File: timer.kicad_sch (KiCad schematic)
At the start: 9 parts, among them Q1 PN2222A, U33 8254, U4 74LS00, U41 74LS175

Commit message: fixed things
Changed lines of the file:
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@@
 	)
 	(hierarchical_label "PIT IRQ"
-		(shape input)
+		(shape output)
 		(at 208.28 106.68 0)
 		(effects
@@
 	)
 	(hierarchical_label "SPKR OUT"
-		(shape input)
+		(shape output)
 		(at 208.28 140.97 0)
 		(effects

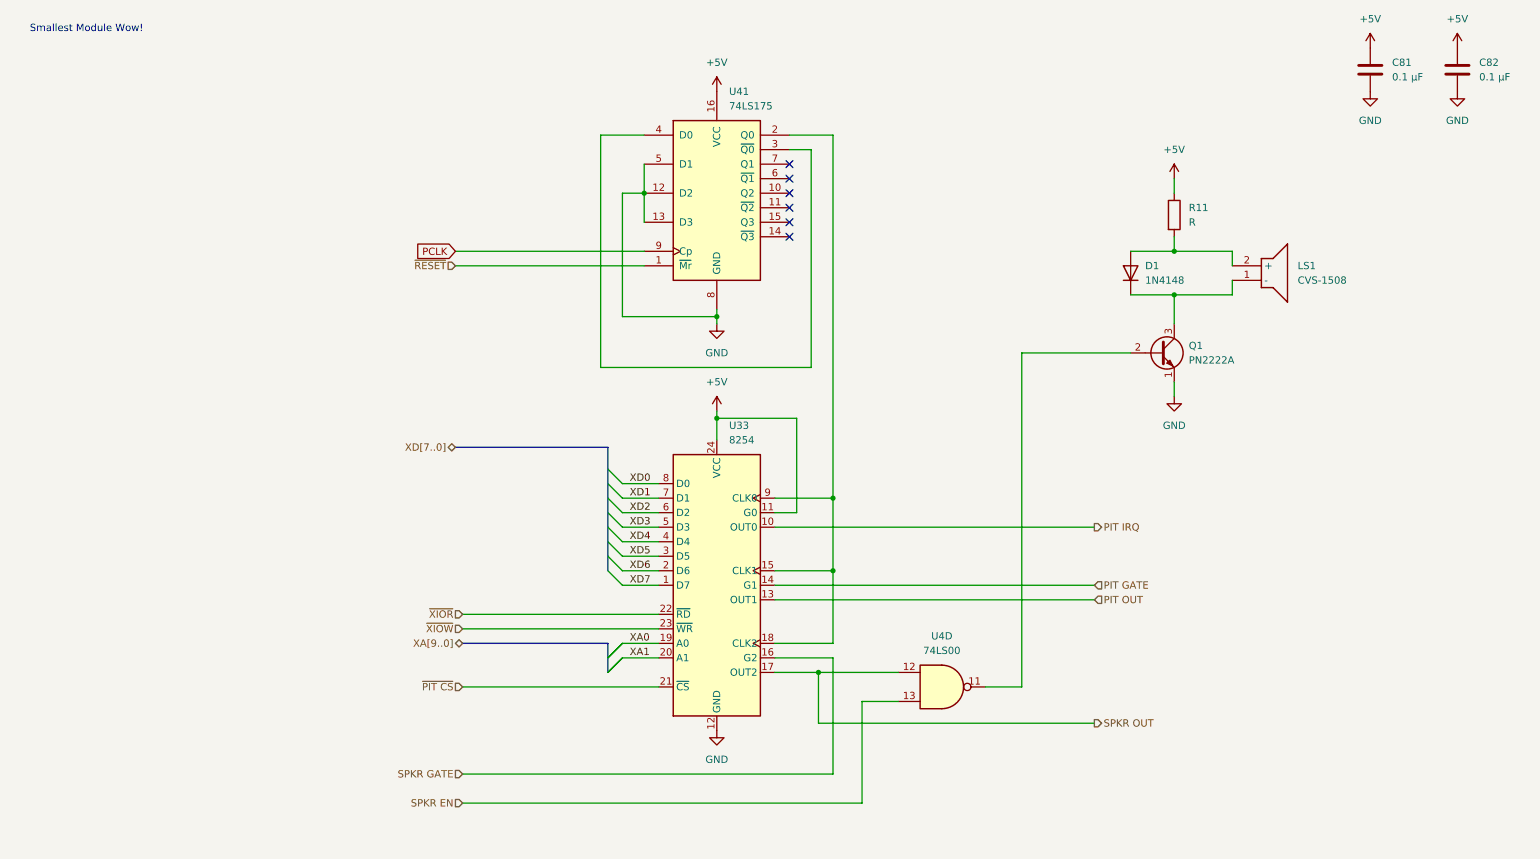
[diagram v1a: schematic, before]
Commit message: Upgraded speaker, esd protection, added dip sockets, adjusted routing
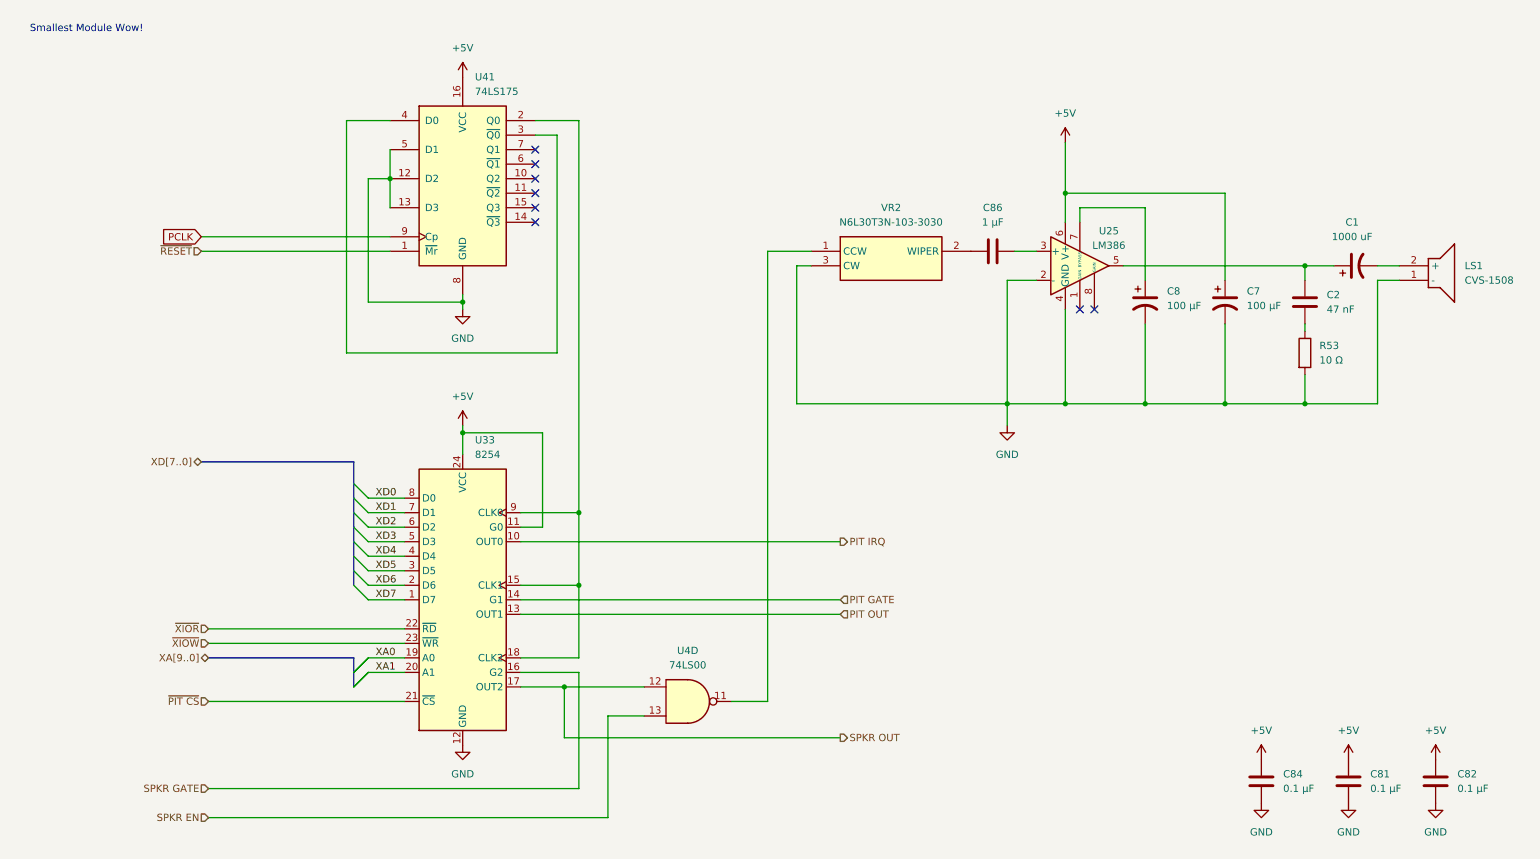
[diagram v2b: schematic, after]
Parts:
- removed D1: 1N4148, Diode_THT:D_DO-35_SOD27_P7.62mm_Horizontal, symbol Diode:1N4148
- removed Q1: PN2222A, Package_TO_SOT_THT:TO-92_Inline, symbol Transistor_BJT:PN2222A
- removed R11: R, Resistor_SMD:R_1206_3216Metric_Pad1.30x1.75mm_HandSolder, symbol Device:R
- added C1: 1000 uF, Capacitor_THT:CP_Radial_D8.0mm_P3.50mm, symbol Device:C_Polarized_US
- added C2: 47 nF, Capacitor_SMD:C_1210_3225Metric_Pad1.33x2.70mm_HandSolder, symbol Device:C
- added C7, C8: 100 μF, Capacitor_THT:CP_Radial_D6.3mm_P2.50mm, symbol Device:C_Polarized_US
- added C84: 0.1 μF, Capacitor_SMD:C_1210_3225Metric_Pad1.33x2.70mm_HandSolder, symbol Device:C
- added C86: 1 μF, Capacitor_SMD:C_1210_3225Metric_Pad1.33x2.70mm_HandSolder, symbol Device:C
- added R53: 10 Ω, Resistor_SMD:R_1206_3216Metric_Pad1.30x1.75mm_HandSolder, symbol Device:R
- added U25: LM386, Package_DIP:DIP-8_W7.62mm_Socket, symbol Amplifier_Audio:LM386
- added VR2: N6L30T3N-103-3030, Library:N6L30T3N1033030, symbol N6L30T3N-103-3030:N6L30T3N-103-3030
- U33: footprint Package_DIP:DIP-24_W15.24mm -> Package_DIP:DIP-24_W15.24mm_Socket
- U4: footprint Package_DIP:DIP-14_W7.62mm -> Package_DIP:DIP-14_W7.62mm_Socket
- U41: footprint Package_DIP:DIP-16_W7.62mm -> Package_DIP:DIP-16_W7.62mm_Socket
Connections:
- net +5V: now also C7.1, C84.1, U25.6 (V+)
- net GND: now also LS1.1 (-), C7.2, C8.2, C84.2, R53.2, U25.2 (-), U25.4 (GND), VR2.3 (CW)
- net at LS1.2 (+): now also C1.2
- net at U4.11: now also VR2.1 (CCW)
- new net: C86.1, VR2.2 (WIPER)
- new net: C86.2, U25.3 (+)
- new net: C1.1, C2.1, U25.5
- new net: C8.1, U25.7 (BYPASS)
- new net: C2.2, R53.1
- no-connect marks 6 -> 8
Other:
- moved on the sheet: C81, C82, LS1, U33, U41, U4D

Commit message: final commit before spinning
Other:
- moved on the sheet: C81, C82, C84
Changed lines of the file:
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@@
 	)
 	(junction
-		(at 85.09 45.72)
+		(at 97.79 67.31)
 		(diameter 0)
 		(color 0 0 0 0)
@@
 	)
 	(junction
-		(at 115.57 134.62)
+		(at 85.09 45.72)
 		(diameter 0)
 		(color 0 0 0 0)
 	)
 	(junction
-		(at 217.17 85.09)
+		(at 115.57 134.62)
 		(diameter 0)
 		(color 0 0 0 0)
 	)
 	(junction
-		(at 97.79 67.31)
+		(at 217.17 85.09)
 		(diameter 0)
 		(color 0 0 0 0)
@@
 	)
 	(hierarchical_label "PIT OUT"
-		(shape input)
+		(shape output)
 		(at 163.83 121.92 0)
 		(effects
@@
 	(symbol
 		(lib_id "power:GND")
-		(at 267.97 154.94 0)
+		(at 269.24 156.21 0)
 		(unit 1)
 		(body_style 1)
@@
 		(fields_autoplaced yes)
 		(property "Reference" "#PWR0272"
-			(at 267.97 161.29 0)
+			(at 269.24 162.56 0)
 			(hide yes)
 			(show_name no)
@@
 		)
 		(property "Value" "GND"
-			(at 267.97 160.02 0)
+			(at 269.24 161.29 0)
 			(show_name no)
 			(do_not_autoplace no)
@@
 		)
 		(property "Footprint" ""
-			(at 267.97 154.94 0)
+			(at 269.24 156.21 0)
 			(hide yes)
 			(show_name no)
@@
 		)
 		(property "Datasheet" ""
-			(at 267.97 154.94 0)
+			(at 269.24 156.21 0)
 			(hide yes)
 			(show_name no)
@@
 		)
 		(property "Description" "Power symbol creates a global label with name \"GND\" , ground"
-			(at 267.97 154.94 0)
+			(at 269.24 156.21 0)
 			(hide yes)
 			(show_name no)
@@
 	(symbol
 		(lib_id "power:GND")
-		(at 252.73 154.94 0)
+		(at 254 156.21 0)
 		(unit 1)
 		(body_style 1)
@@
 		(fields_autoplaced yes)
 		(property "Reference" "#PWR0270"
-			(at 252.73 161.29 0)
+			(at 254 162.56 0)
 			(hide yes)
 			(show_name no)
@@
 		)
 		(property "Value" "GND"
-			(at 252.73 160.02 0)
+			(at 254 161.29 0)
 			(show_name no)
 			(do_not_autoplace no)
@@
 		)
 		(property "Footprint" ""
-			(at 252.73 154.94 0)
+			(at 254 156.21 0)
 			(hide yes)
 			(show_name no)
@@
 		)
 		(property "Datasheet" ""
-			(at 252.73 154.94 0)
+			(at 254 156.21 0)
 			(hide yes)
 			(show_name no)
@@
 		)
 		(property "Description" "Power symbol creates a global label with name \"GND\" , ground"
-			(at 252.73 154.94 0)
+			(at 254 156.21 0)
 			(hide yes)
 			(show_name no)
@@
 	(symbol
 		(lib_id "Device:C")
-		(at 267.97 151.13 0)
+		(at 269.24 152.4 0)
 		(unit 1)
 		(body_style 1)
@@
 		(fields_autoplaced yes)
 		(property "Reference" "C82"
-			(at 271.78 149.8599 0)
+			(at 273.05 151.1299 0)
 			(show_name no)
 			(do_not_autoplace no)
@@
 		)
 		(property "Value" "0.1 μF"
-			(at 271.78 152.3999 0)
+			(at 273.05 153.6699 0)
 			(show_name no)
 			(do_not_autoplace no)
@@
 		)
 		(property "Footprint" "Capacitor_SMD:C_1210_3225Metric_Pad1.33x2.70mm_HandSolder"
-			(at 268.9352 154.94 0)
+			(at 270.2052 156.21 0)
 			(hide yes)
 			(show_name no)
@@
 		)
 		(property "Datasheet" ""
-			(at 267.97 151.13 0)
+			(at 269.24 152.4 0)
 			(hide yes)
 			(show_name no)
@@
 		)
 		(property "Description" "Unpolarized capacitor"
-			(at 267.97 151.13 0)
+			(at 269.24 152.4 0)
 			(hide yes)
 			(show_name no)
@@
 		)
 		(property "Sim.Type" ""
-			(at 267.97 151.13 0)
+			(at 269.24 152.4 0)
 			(hide yes)
 			(show_name no)
@@
 		)
 		(property "Sim.Device" ""
-			(at 267.97 151.13 0)
+			(at 269.24 152.4 0)
 			(hide yes)
 			(show_name no)
@@
 	(symbol
 		(lib_id "power:GND")
-		(at 237.49 154.94 0)
+		(at 238.76 156.21 0)
 		(unit 1)
 		(body_style 1)
@@
 		(fields_autoplaced yes)
 		(property "Reference" "#PWR0279"
-			(at 237.49 161.29 0)
+			(at 238.76 162.56 0)
 			(hide yes)
 			(show_name no)
@@
 		)
 		(property "Value" "GND"
-			(at 237.49 160.02 0)
+			(at 238.76 161.29 0)
 			(show_name no)
 			(do_not_autoplace no)
@@
 		)
 		(property "Footprint" ""
-			(at 237.49 154.94 0)
+			(at 238.76 156.21 0)
 			(hide yes)
 			(show_name no)
@@
 		)
 		(property "Datasheet" ""
-			(at 237.49 154.94 0)
+			(at 238.76 156.21 0)
 			(hide yes)
 			(show_name no)
@@
 		)
 		(property "Description" "Power symbol creates a global label with name \"GND\" , ground"
-			(at 237.49 154.94 0)
+			(at 238.76 156.21 0)
 			(hide yes)
 			(show_name no)
@@
 	(symbol
 		(lib_id "power:VCC")
-		(at 237.49 147.32 0)
+		(at 238.76 148.59 0)
 		(unit 1)
 		(body_style 1)
@@
 		(fields_autoplaced yes)
 		(property "Reference" "#PWR0278"
-			(at 237.49 151.13 0)
+			(at 238.76 152.4 0)
 			(hide yes)
 			(show_name no)
@@
 		)
 		(property "Value" "+5V"
-			(at 237.49 142.24 0)
+			(at 238.76 143.51 0)
 			(show_name no)
 			(do_not_autoplace no)
@@
 		)
 		(property "Footprint" ""
-			(at 237.49 147.32 0)
+			(at 238.76 148.59 0)
 			(hide yes)
 			(show_name no)
@@
 		)
 		(property "Datasheet" ""
-			(at 237.49 147.32 0)
+			(at 238.76 148.59 0)
 			(hide yes)
 			(show_name no)
@@
 		)
 		(property "Description" "Power symbol creates a global label with name \"VCC\""
-			(at 237.49 147.32 0)
+			(at 238.76 148.59 0)
 			(hide yes)
 			(show_name no)
@@
 	(symbol
 		(lib_id "power:VCC")
-		(at 267.97 147.32 0)
+		(at 269.24 148.59 0)
 		(unit 1)
 		(body_style 1)
@@
 		(fields_autoplaced yes)
 		(property "Reference" "#PWR0271"
-			(at 267.97 151.13 0)
+			(at 269.24 152.4 0)
 			(hide yes)
 			(show_name no)
@@
 		)
 		(property "Value" "+5V"
-			(at 267.97 142.24 0)
+			(at 269.24 143.51 0)
 			(show_name no)
 			(do_not_autoplace no)
@@
 		)
 		(property "Footprint" ""
-			(at 267.97 147.32 0)
+			(at 269.24 148.59 0)
 			(hide yes)
 			(show_name no)
@@
 		)
 		(property "Datasheet" ""
-			(at 267.97 147.32 0)
+			(at 269.24 148.59 0)
 			(hide yes)
 			(show_name no)
@@
 		)
 		(property "Description" "Power symbol creates a global label with name \"VCC\""
-			(at 267.97 147.32 0)
+			(at 269.24 148.59 0)
 			(hide yes)
 			(show_name no)
@@
 	(symbol
 		(lib_id "power:VCC")
-		(at 252.73 147.32 0)
+		(at 254 148.59 0)
 		(unit 1)
 		(body_style 1)
@@
 		(fields_autoplaced yes)
 		(property "Reference" "#PWR0269"
-			(at 252.73 151.13 0)
+			(at 254 152.4 0)
 			(hide yes)
 			(show_name no)
@@
 		)
 		(property "Value" "+5V"
-			(at 252.73 142.24 0)
+			(at 254 143.51 0)
 			(show_name no)
 			(do_not_autoplace no)
@@
 		)
 		(property "Footprint" ""
-			(at 252.73 147.32 0)
+			(at 254 148.59 0)
 			(hide yes)
 			(show_name no)
@@
 		)
 		(property "Datasheet" ""
-			(at 252.73 147.32 0)
+			(at 254 148.59 0)
 			(hide yes)
 			(show_name no)
@@
 		)
 		(property "Description" "Power symbol creates a global label with name \"VCC\""
-			(at 252.73 147.32 0)
+			(at 254 148.59 0)
 			(hide yes)
 			(show_name no)
@@
 	(symbol
 		(lib_id "Device:C")
-		(at 237.49 151.13 0)
+		(at 238.76 152.4 0)
 		(unit 1)
 		(body_style 1)
@@
 		(fields_autoplaced yes)
 		(property "Reference" "C84"
-			(at 241.3 149.8599 0)
+			(at 242.57 151.1299 0)
 			(show_name no)
 			(do_not_autoplace no)
@@
 		)
 		(property "Value" "0.1 μF"
-			(at 241.3 152.3999 0)
+			(at 242.57 153.6699 0)
 			(show_name no)
 			(do_not_autoplace no)
@@
 		)
 		(property "Footprint" "Capacitor_SMD:C_1210_3225Metric_Pad1.33x2.70mm_HandSolder"
-			(at 238.4552 154.94 0)
+			(at 239.7252 156.21 0)
 			(hide yes)
 			(show_name no)
@@
 		)
 		(property "Datasheet" ""
-			(at 237.49 151.13 0)
+			(at 238.76 152.4 0)
 			(hide yes)
 			(show_name no)
@@
 		)
 		(property "Description" "Unpolarized capacitor"
-			(at 237.49 151.13 0)
+			(at 238.76 152.4 0)
 			(hide yes)
 			(show_name no)
@@
 		)
 		(property "Sim.Type" ""
-			(at 237.49 151.13 0)
+			(at 238.76 152.4 0)
 			(hide yes)
 			(show_name no)
@@
 		)
 		(property "Sim.Device" ""
-			(at 237.49 151.13 0)
+			(at 238.76 152.4 0)
 			(hide yes)
 			(show_name no)
@@
 	(symbol
 		(lib_id "Device:C")
-		(at 252.73 151.13 0)
+		(at 254 152.4 0)
 		(unit 1)
 		(body_style 1)
@@
 		(fields_autoplaced yes)
 		(property "Reference" "C81"
-			(at 256.54 149.8599 0)
+			(at 257.81 151.1299 0)
 			(show_name no)
 			(do_not_autoplace no)
@@
 		)
 		(property "Value" "0.1 μF"
-			(at 256.54 152.3999 0)
+			(at 257.81 153.6699 0)
 			(show_name no)
 			(do_not_autoplace no)
@@
 		)
 		(property "Footprint" "Capacitor_SMD:C_1210_3225Metric_Pad1.33x2.70mm_HandSolder"
-			(at 253.6952 154.94 0)
+			(at 254.9652 156.21 0)
 			(hide yes)
 			(show_name no)
@@
 		)
 		(property "Datasheet" ""
-			(at 252.73 151.13 0)
+			(at 254 152.4 0)
 			(hide yes)
 			(show_name no)
@@
 		)
 		(property "Description" "Unpolarized capacitor"
-			(at 252.73 151.13 0)
+			(at 254 152.4 0)
 			(hide yes)
 			(show_name no)
@@
 		)
 		(property "Sim.Type" ""
-			(at 252.73 151.13 0)
+			(at 254 152.4 0)
 			(hide yes)
 			(show_name no)
@@
 		)
 		(property "Sim.Device" ""
-			(at 252.73 151.13 0)
+			(at 254 152.4 0)
 			(hide yes)
 			(show_name no)
